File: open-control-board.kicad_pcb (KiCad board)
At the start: 4 copper layers, 69 x 109 mm, 140 parts, among them CN1 Service boiler fill sensor, CN10 LCC Port, CN2 Water tank level switch, CN3 NTC Service Boiler, CN4 NTC Brew Boiler, CN5 Service boiler relay, CN6 Conn_02x04_Counter_Clockwise, CN7 Brew Switch, CN8 12V Separate Supply, CN9 Brew boiler relay, J1 USB_B_Micro, J10 Conn_01x04_Pin, J11 Conn_01x04_Pin, J12 Conn_02x06_Odd_Even, J13 Conn_02x05_Odd_Even, J14 Conn_02x04_Odd_Even, J15 Conn_02x05_Odd_Even, J16 USB_B_Micro, J17 BM04B-SRSS-TB(LF)(SN), J2 BM04B-SRSS-TB(LF)(SN), J3 Conn_01x01_Pin, J4 Conn_01x01_Pin, J5 Conn_01x01_Pin, J6 Conn_01x01_Pin, J7 Conn_01x01_Pin, J8 Conn_01x01_Pin, J9 ECE05US05, K1 RT314A12, Q1 AO3401A, Q2 AO3401A, Q3 AO3401A, Q4 AO3401A, Q5 AO3401A, SW1 SW_Push, SW2 SW_Push, SW3 SW_Push, SW4 SW_Push, U1 TPS82130, U10 FDC1004, U11 ALDP112, U12 ALDP112, U13 ALDP112, U15 STPIC6C595TTR, U16 STPIC6C595TTR, U2 MCP7940N-xSN, U3 TPS82130, U4 RP2040, U5 ESP32-S3-WROOM-1, U7 TXB0108DQSR, U8 ADS1115IDGS, U9 W25Q16JVUXIQ, Y1 XYDBPCNANF-12MHZ, Y3 YSX1610SK, 9 pF

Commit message: WIP
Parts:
- added locked: VAL**, Panelization:mouse-bite-2mm-slot, F.Cu at (55.8, 79.5)
- added mouse-bite-2mm-slot: VAL**, Panelization:mouse-bite-2mm-slot, F.Cu at (96.8, 79.5)
- added mouse-bite-2mm-slot: VAL**, Panelization:mouse-bite-2mm-slot, F.Cu at (75.2, 79.5)
- added mouse-bite-2mm-slot: VAL**, Panelization:mouse-bite-2mm-slot, F.Cu at (117.3, 79.5)
- C32: value 22 uF, 10V, X5R -> 22 uF, 6.3V, X5R
- FB1, FB2: footprint PCM_Ferrite_SMD_AKL:Ferrite_0402_1005Metric -> PCM_Ferrite_SMD_AKL:Ferrite_0603_1608Metric
- J3, J4, J5, J6, J7, J8: footprint Connector_Pin:Pin_D1.4mm_L8.5mm_W2.8mm_FlatFork -> 1289:KEYSTONE_1289
- moved J8 5.02 mm to (110.0, 128.6), turned to 90 degrees
- moved J5 4.45 mm to (68.6, 128.6), turned to 90 degrees
- moved F1 1.00 mm to (110.0, 121.0)
- moved J9 1.00 mm to (98.1, 113.8)
- moved JP1 1.00 mm to (54.3, 83.0)
- moved K1 1.00 mm to (56.2, 91.8)
- moved U11 1.00 mm to (90.8, 115.8)
- moved U12 1.00 mm to (82.3, 115.8)
- moved U13 1.00 mm to (73.8, 115.8)
- moved C29 0.93 mm to (97.3, 32.8)
- moved R27 0.92 mm to (100.8, 33.6)
- moved J6 0.89 mm to (56.2, 128.4), turned to 90 degrees
- moved J4 0.80 mm to (82.7, 129.2), turned to 90 degrees
- moved J7 0.77 mm to (103.2, 128.8), turned to 90 degrees
- moved FB2 0.68 mm to (98.5, 35.0)
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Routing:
- net +3V3: track 271.6 -> 321.3 mm, vias 11 -> 12
- net GND: track 99.9 -> 119.4 mm, vias 50 -> 34
- net nG_5V: track 8.97 -> 19.8 mm
- net ESP32_RP2040_UART2: track 17.8 -> 26.2 mm
- net SRCLR_5V: track 10.7 -> 18.9 mm
- net CN6_3_5V: track 25.7 -> 33.6 mm
- net CN6_2_5V: track 21.3 -> 28.7 mm
- net WATER_TANK_LVL_SW: track 16.4 -> 23.0 mm, vias 1 -> 2
- net RCLK_5V: track 11.5 -> 18.0 mm
- net GP27: track 36.3 -> 42.5 mm
- net GP26: track 40.9 -> 47.0 mm
- net SRCK_3V3: track 25.1 -> 31.0 mm
- net SRCK_5V: track 14.1 -> 19.6 mm, vias 2 -> 0
- net SRCLR_3V3: track 22.0 -> 27.4 mm
- net SER_IN_3V3: track 22.9 -> 28.0 mm
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- added copper zone on In2.Cu, net GND
- removed copper zone on In2.Cu, net (none)
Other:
- board size 69 x 109 mm -> 69 x 110 mm

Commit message: WIP
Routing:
- net Net-(U16-DRAIN1): track 50.5 -> 47.8 mm
- net SRCK_5V: track 19.6 -> 17.2 mm
- net SRCK_3V3: track 31.0 -> 33.3 mm
- net nG_5V: track 19.8 -> 17.7 mm
- net GP21: track 49.2 -> 47.7 mm
- net SRCLR_5V: track 18.9 -> 20.2 mm
- net Net-(U15-DRAIN1): track 45.9 -> 44.7 mm
- net CN10_12V_GATE: track 50.9 -> 49.8 mm
- net Net-(U16-DRAIN0): track 36.5 -> 35.5 mm
- net ESP32_RP2040_UART1: track 34.7 -> 33.6 mm, vias 4 -> 2
- net CN10_UART_RX: track 69.9 -> 68.9 mm
- net RP2040_BOOTSEL: track 29.0 -> 29.8 mm
- net ESP32_EN: track 47.6 -> 46.9 mm
- net Net-(U15-DRAIN5): track 6.32 -> 5.56 mm
- net RCLK_3V3: track 23.0 -> 22.4 mm
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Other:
- board text added: "12V"
- board text added: "3V3"
- board text added: "5V"
- board text added: "AGND"
- board text added: "AVCC"
- board text added: "ESP32 EN"
- board text added: "ESP32 GPIO0"
- board text added: "ESP32 JTAG"
- board text added: "ESP32 JTAG Source"
- board text added: "ESP32 QWIIC"
- board text added: "ESP32 USB"
- board text added: "GND"
- board text added: "RP2040 Boot"
- board text added: "RP2040 DBG"
- board text added: "RP2040 QWIIC"
- board text added: "RP2040 Reset"
- board text added: "RP2040 USB"
- board text added: "USB 5V"
- board text added: "VOUT1 V"
- board text added: "VOUT2 V"
- board text added: "VOUT3 V"

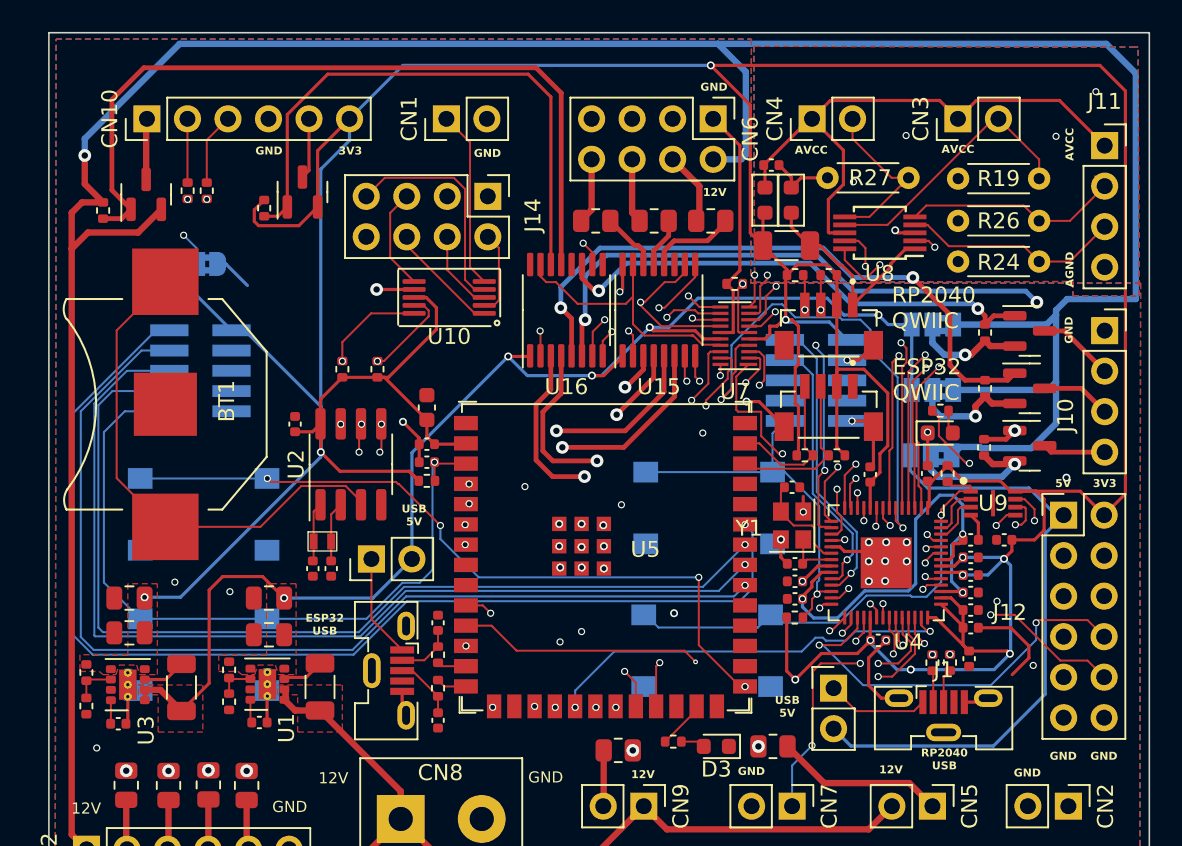
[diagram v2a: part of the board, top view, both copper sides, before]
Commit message: Added possibility to select CN10 levels via solder jumpers
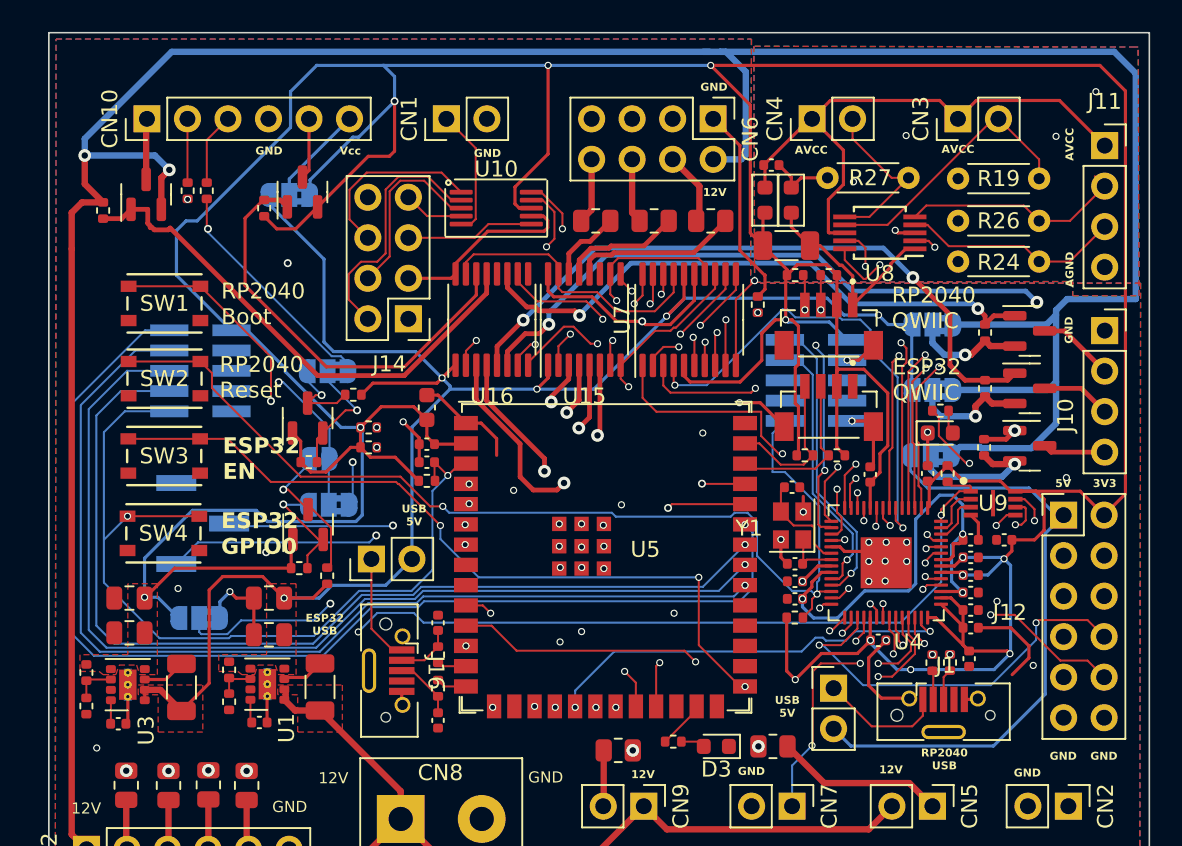
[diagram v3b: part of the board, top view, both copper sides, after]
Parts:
- removed BT1: Battery_Cell, BK-885:BAT_BK-885
- removed C24, C25: 11 pF, Capacitor_SMD:C_0402_1005Metric
- removed C26: 100 nF, 50V, X7R, Capacitor_SMD:C_0402_1005Metric
- removed U2: MCP7940N-xSN, Package_SO:SOP-8_3.76x4.96mm_P1.27mm
- removed Y3: YSX1610SK, 9 pF, SMD1610-2P:SMD1610-2P
- added J18: Conn_01x03_Pin, Connector_PinHeader_2.54mm:PinHeader_1x03_P2.54mm_Vertical_SMD_Pin1Left, B.Cu at (61.6, 55.3)
- added JP10: SolderJumper_3_Bridged12, Jumper:SolderJumper-3_P1.3mm_Bridged2Bar12_RoundedPad1.0x1.5mm_NumberLabels, B.Cu at (69.5, 45.7)
- added JP11: SolderJumper_3_Bridged12, Jumper:SolderJumper-3_P1.3mm_Bridged2Bar12_RoundedPad1.0x1.5mm_NumberLabels, B.Cu at (69.5, 54.1)
- added JP12: SolderJumper_2_Open, Jumper:SolderJumper-2_P1.3mm_Open_RoundedPad1.0x1.5mm, B.Cu at (68.9, 51.2)
- added JP9: SolderJumper_3_Bridged12, Jumper:SolderJumper-3_P1.3mm_Bridged2Bar12_RoundedPad1.0x1.5mm_NumberLabels, B.Cu at (67.1, 34.7)
- added Q6: 2N7002, Package_TO_SOT_SMD:SOT-23, F.Cu at (68.2, 48.7)
- added Q7: 2N7002, Package_TO_SOT_SMD:SOT-23, F.Cu at (68.2, 55.3)
- added R41: 10K, Resistor_SMD:R_0402_1005Metric, F.Cu at (68.3, 51.4)
- added R42: 10K, Resistor_SMD:R_0402_1005Metric, F.Cu at (71.1, 47.2)
- added R43: 10K, Resistor_SMD:R_0402_1005Metric, F.Cu at (67.7, 58.1)
- added R44: 10K, Resistor_SMD:R_0402_1005Metric, F.Cu at (69.5, 58.5)
- J1, J16: footprint Connector_USB:USB_Micro-B_Molex-105133-0031 -> U-D-M5DS-W-3:U-D-M5DS-W-3
- JP4, JP5, JP6: footprint Jumper:SolderJumper-3_P1.3mm_Bridged2Bar12_Pad1.0x1.5mm_NumberLabels -> Jumper:SolderJumper-3_P1.3mm_Bridged2Bar12_RoundedPad1.0x1.5mm_NumberLabels
- SW1, SW2, SW3, SW4: footprint Button_Switch_SMD:SW_SPST_B3S-1000 -> ul_PTS815-SJM-250-SMTR-LFS:SW4_PTS815 SJM 250 SMTR LFS_CNK; moved to F.Cu
- U7: value TXB0108DQSR -> TXB0108PWR; footprint Package_SON:USON-20_2x4mm_P0.4mm -> Package_SO:TSSOP-20_4.4x6.5mm_P0.65mm
- moved SW1 40.4 mm to (59.2, 41.5), turned to 0 degrees
- moved SW2 35.1 mm to (59.3, 46.2), turned to 0 degrees
- moved JP8 22.2 mm to (61.4, 61.2)
- moved J14 9.15 mm to (74.5, 42.4), turned to 180 degrees
- moved SW4 8.01 mm to (59.2, 55.9), turned to 0 degrees
- moved U10 6.33 mm to (80.0, 35.5), turned to 0 degrees
- moved R21 4.93 mm to (72.0, 50.5), turned to 180 degrees
- moved U15 4.71 mm to (85.6, 42.5)
- moved U16 4.71 mm to (79.8, 42.5)
- moved SW3 4.41 mm to (59.2, 51.0), turned to 0 degrees
- moved R20 4.01 mm to (72.0, 49.2), turned to 180 degrees
- moved U7 3.03 mm to (92.2, 42.5), turned to 90 degrees
- moved R31 1.95 mm to (96.5, 41.5), turned to 90 degrees
- moved J16 1.25 mm to (72.1, 64.5)
- moved J1 1.05 mm to (108.1, 68.3)
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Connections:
- CN10 pad 6: +3V3 -> Net-(CN10-Pin_6)
- R5 pad 2: CN10_UART_TX -> CN10_UART_RX
- R6 pad 2: CN10_UART_RX -> CN10_UART_TX_SHIFT_SEL
- U4 pad 18: RTC_MFP -> GP15
- U4 pad 28: CN10_UART_RX -> CN10_UART_RX_SHIFT_SEL
- U5 pad 10: CN10_UART_RX -> CN10_UART_RX_SHIFT_SEL
- U5 pad 36: ESP32_RXD0 -> Net-(J18-Pin_1)
- U5 pad 37: ESP32_TXD0 -> Net-(J18-Pin_2)
- U5 pad 8: ESP32_RTS0 -> unconnected-(U5-GPIO15/U0RTS/ADC2_CH4/XTAL_32K_P-Pad8)
- U5 pad 9: ESP32_CTS0 -> unconnected-(U5-GPIO16/U0CTS/ADC2_CH5/XTAL_32K_N-Pad9)
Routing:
- net CN10_UART_RX_SHIFT_SEL: track 0.00 -> 56.3 mm, vias 0 -> 4
- net RP2040_BOOTSEL: track 29.8 -> 77.8 mm, vias 1 -> 3
- net CN10_UART_RX: track 68.9 -> 23.0 mm, vias 4 -> 2
- net RP2040_RESETn: track 23.7 -> 67.0 mm, vias 1 -> 2
- net Net-(J18-Pin_1): track 0.00 -> 39.8 mm, vias 0 -> 2
- net +3V3: track 321.2 -> 358.1 mm, vias 12 -> 14
- net RTC_MFP: track 36.3 -> 0.00 mm, vias 2 -> 0
- net Net-(J18-Pin_2): track 0.00 -> 35.0 mm, vias 0 -> 2
- net GND: track 119.1 -> 153.7 mm, vias 34 -> 35
- net Net-(BT1-+): track 32.1 -> 0.00 mm
- net +5V: track 125.5 -> 151.3 mm
- net CN10_12V_GATE: track 49.8 -> 32.6 mm
- net CN10_UART_TX_SHIFT_SEL: track 0.00 -> 14.8 mm, vias 0 -> 1
- net ESP32_JTAG_SELECT: track 39.8 -> 28.2 mm
- net CIN1: track 5.32 -> 15.8 mm
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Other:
- board text added: "Bridged = 5V"
- board text added: "CN10 RX V"
- board text added: "CN10 TX V"
- board text added: "CN10 Vcc"
- board text added: "RX"
- board text added: "TX"
- board text added: "UART"
- board text added: "Vcc"

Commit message: WIP
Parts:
- removed JP10, JP11: SolderJumper_3_Bridged12, Jumper:SolderJumper-3_P1.3mm_Bridged2Bar12_RoundedPad1.0x1.5mm_NumberLabels
- removed JP12: SolderJumper_2_Open, Jumper:SolderJumper-2_P1.3mm_Open_RoundedPad1.0x1.5mm
- removed Q7: 2N7002, Package_TO_SOT_SMD:SOT-23
- removed R41, R42, R43, R44: 10K, Resistor_SMD:R_0402_1005Metric
- added JP13: SolderJumper_3_Bridged12, Jumper:SolderJumper-3_P1.3mm_Bridged2Bar12_RoundedPad1.0x1.5mm_NumberLabels, B.Cu at (98.3, 37.0)
- added Q11: DMN63D8LDW, PCM_Package_TO_SOT_SMD_AKL:SOT-363_SC-70-6, F.Cu at (61.8, 34.7)
- added R49: 10K, Resistor_SMD:R_0402_1005Metric, F.Cu at (115.3, 42.1)
- added R50: 10K, Resistor_SMD:R_0402_1005Metric, F.Cu at (113.3, 39.9)
- added REF**: OSHW-Logo2_14.6x12mm_SilkScreen, Symbol:OSHW-Logo2_14.6x12mm_SilkScreen, F.Cu at (83.5, 89.0)
- added REF**: OSHW-Logo2_7.3x6mm_Copper, Symbol:OSHW-Logo2_7.3x6mm_Copper, B.Cu at (57.2, 37.9)
- added RN1: 10K, PCM_Resistor_SMD_AKL:R_Array_Concave_4x0402, F.Cu at (61.9, 37.3)
- added RN2: 10K, PCM_Resistor_SMD_AKL:R_Array_Concave_4x0402, F.Cu at (113.3, 41.7)
- Q3, Q5: value AO3401A -> Q_PMOS-E_DUAL_Generic_SEP_S1G1D2S2G2D1; footprint Package_TO_SOT_SMD:SOT-23 -> PCM_Package_TO_SOT_SMD_AKL:Vishay_PowerPAK_SC70-6L_Dual
- Q4: value AO3401A -> DMN63D8LDW; footprint Package_TO_SOT_SMD:SOT-23 -> PCM_Package_TO_SOT_SMD_AKL:SOT-363_SC-70-6
- Q6: value 2N7002 -> DMN63D8LDW; footprint Package_TO_SOT_SMD:SOT-23 -> PCM_Package_TO_SOT_SMD_AKL:SOT-363_SC-70-6
- moved Q6 39.8 mm to (107.5, 42.0)
- moved R29 6.75 mm to (114.5, 52.4), turned to 0 degrees
- moved R30 4.76 mm to (114.9, 48.4), turned to 180 degrees
- moved R28 4.35 mm to (115.0, 44.2), turned to 180 degrees
- moved Q5 4.21 mm to (114.6, 46.3), turned to 90 degrees
- moved Q3 3.83 mm to (114.6, 50.5), turned to 90 degrees
- moved Q4 3.32 mm to (110.4, 42.0), turned to 90 degrees
- moved JP6 2.79 mm to (110.1, 51.2)
- moved JP4 2.74 mm to (110.0, 43.6)
- moved JP5 2.69 mm to (110.0, 47.4)
- moved R6 2.04 mm to (62.9, 32.6), turned to 180 degrees
- moved R5 1.77 mm to (60.9, 32.6), turned to 0 degrees
- moved R24 0.68 mm to (109.0, 38.2)
- moved R19 0.38 mm to (109.0, 35.9)
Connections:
- net Net-(CN10-Pin_6) renamed CN10_UART_VCC
- C28 pad 1: +3V3 -> Net-(JP13-C)
- FB1 pad 2: +3V3 -> Net-(JP13-C)
- J12 pad 1: +5V -> +3V3
- Q3 pad 1: VOUT_2_GATE -> Net-(JP5-C)
- Q3 pad 2: Net-(JP5-C) -> VOUT_2_GATE
- Q3 pad 3: VOUT_2 -> VOUT_3
- Q4 pad 1: VOUT_1_GATE -> ADS1115_RDY
- Q4 pad 2: Net-(JP4-C) -> +3V3
- Q4 pad 3: VOUT_1 -> unconnected-(Q4B-D2-Pad3)
- Q5 pad 1: VOUT_3_GATE -> (no net)
- Q5 pad 2: Net-(JP6-C) -> (no net)
- Q5 pad 3: VOUT_3 -> VOUT_1
- Q6 pad 1: +3V3 -> INT_SDA
- Q6 pad 2: CN10_UART_TX -> +3V3
- Q6 pad 3: Net-(JP10-B) -> INT_SCL_AVCC
- U8 pad 1: GND -> AGND
- U8 pad 10: INT_SCL -> INT_SCL_AVCC
- U8 pad 2: ADS1115_RDY -> ADS1115_RDY_AVCC
- U8 pad 9: INT_SDA -> INT_SDA_AVCC
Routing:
- net AGND: track 5.56 -> 25.2 mm
- net CN10_UART_RX_SHIFT_SEL: track 56.3 -> 75.6 mm
- net VOUT_2_GATE: track 41.7 -> 60.6 mm
- net CN10_UART_RX: track 23.0 -> 5.28 mm, vias 2 -> 0
- net +12V: track 249.6 -> 233.2 mm
- net INT_SCL_AVCC: track 0.00 -> 14.4 mm, vias 0 -> 2
- net AVCC: track 37.0 -> 51.3 mm
- net INT_SDA_AVCC: track 0.00 -> 14.3 mm, vias 0 -> 2
- net CN10_UART_TX: track 61.7 -> 73.2 mm, vias 4 -> 5
- net CN10_UART_VCC: track 6.66 -> 17.2 mm, vias 0 -> 1
- net ADS1115_RDY_AVCC: track 0.00 -> 9.31 mm
- net Net-(JP12-B): track 9.17 -> 0.00 mm, vias 1 -> 0
- net VOUT_3_GATE: track 49.2 -> 56.5 mm, vias 3 -> 2
- net Net-(JP11-B): track 7.18 -> 0.00 mm, vias 1 -> 0
- net VOUT_1_GATE: track 36.9 -> 43.6 mm
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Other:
- board text added: "ADC Vcc"
- board text added: "All-Purpose Espresso Controller HV board"
- board text added: "All-Purpose Espresso Controller Main board"
- board text added: "Are there reasonable fuses for this footprint?"
- board text added: "ESP32"
- board text added: "Height???"
- board text added: "RP2040"
- board text added: "Rename connectors and jumpers?"
- board text added: "Rev R0A"
- board text added: "Split ground?"
- board text added: "The drill size looks small, but is according to the Data sheet. Double check though."
- board text added: "This part still needs to be measured to a case"
- board text removed: "Bridged = 5V"
- board text removed: "CN10 RX V"
- board text removed: "CN10 TX V"
- board text removed: "ESP32 QWIIC"
- board text removed: "RP2040 QWIIC"

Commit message: WIP
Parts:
- removed J9: ECE05US05, ECE05:CONN5_05US05_XPP
- removed R14, R15, R16, R25, R3, R38, R39, R4, R40: 480R, 500mW, Resistor_SMD:R_0805_2012Metric
- removed REF**: OSHW-Logo2_14.6x12mm_SilkScreen, Symbol:OSHW-Logo2_14.6x12mm_SilkScreen
- removed REF**: OSHW-Logo2_7.3x6mm_Copper, Symbol:OSHW-Logo2_7.3x6mm_Copper
- added C24: 100 nF, 50V, X7R, Capacitor_SMD:C_0402_1005Metric, F.Cu at (82.3, 32.7)
- added C25: 1 uF, 16V, X5R, Capacitor_SMD:C_0402_1005Metric, F.Cu at (82.4, 33.8)
- added D2: 1N4001, Diode_THT:D_DO-41_SOD81_P7.62mm_Horizontal, F.Cu at (91.3, 93.3)
- added D4: 1N4001, Diode_THT:D_DO-41_SOD81_P7.62mm_Horizontal, F.Cu at (83.3, 89.2)
- added D5: 1N4001, Diode_THT:D_DO-41_SOD81_P7.62mm_Horizontal, F.Cu at (75.9, 93.3)
- added D8: 1N4001, Diode_THT:D_DO-41_SOD81_P7.62mm_Horizontal, F.Cu at (54.6, 87.2)
- added U2: ~, ECE05:ECE10, F.Cu at (119.6, 82.6)
- F1: value Fuse -> Schurter FRT 250T 7100.1009.13; footprint Fuse:Fuse_Bourns_MF-RG700 -> 1289:FRT 250T
- J3, J4, J5, J6, J7, J8: value Conn_01x01_Pin -> TE 160650-2
- Q3, Q5: footprint PCM_Package_TO_SOT_SMD_AKL:Vishay_PowerPAK_SC70-6L_Dual -> PCM_Package_TO_SOT_SMD_AKL:TSOT-23-6
- U9: footprint W25Q16JVUXIQ:SON50P300X200X60-9N -> ul_W25Q16JVUXIQ:W25Q16JVUXIQ_WIN
- moved F1 12.9 mm to (107.1, 133.6), turned to 90 degrees
- moved J3 10.7 mm to (80.0, 129.0)
- moved J4 10.2 mm to (72.5, 129.0)
- moved J7 8.25 mm to (95.0, 129.0)
- moved J6 6.28 mm to (62.5, 129.0)
- moved J8 5.01 mm to (115.0, 129.0)
- moved R30 4.78 mm to (111.2, 51.4), turned to -90 degrees
- moved R28 4.58 mm to (111.0, 46.6), turned to -90 degrees
- moved R29 4.55 mm to (111.2, 49.3), turned to -90 degrees
- moved J5 1.17 mm to (67.5, 129.0)
- moved R35 0.90 mm to (90.3, 68.8)
- moved D3 0.90 mm to (93.0, 69.1)
- moved Q3 0.79 mm to (113.9, 50.9), turned to 0 degrees
- moved U10 0.77 mm to (80.0, 36.3)
- moved Q5 0.66 mm to (114.0, 46.1), turned to 0 degrees
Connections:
- CN1 pad 1: CIN4 -> CIN1
- F1 pad 1: Net-(J8-Pin_1) -> PH_PRE_FUSE
- J14 pad 2: CIN1 -> C_SHIELD_2
- J14 pad 3: GND -> C_SHIELD_2
- J14 pad 4: CIN2 -> CIN4
- J14 pad 5: C_SHIELD_2 -> CIN3
- J14 pad 7: CIN3 -> CIN2
- J14 pad 8: GND -> C_SHIELD_1
- J7 pad 1: N -> PH_PRE_FUSE
- J8 pad 1: Net-(J8-Pin_1) -> N
- Q3 pad 1: Net-(JP5-C) -> VOUT_2_GATE
- Q3 pad 2: VOUT_2_GATE -> Net-(JP6-C)
- Q3 pad 3: VOUT_3 -> VOUT_3_GATE
- Q3 pad 4: Net-(JP6-C) -> VOUT_3
- Q3 pad 5: VOUT_3_GATE -> Net-(JP5-C)
- Q5 pad 2: (no net) -> Net-(JP4-C)
- Q5 pad 3: VOUT_1 -> VOUT_1_GATE
- Q5 pad 4: Net-(JP4-C) -> VOUT_1
- Q5 pad 5: VOUT_1_GATE -> (no net)
- U15 pad 12: Net-(U15-DRAIN5) -> CN6_4
- U15 pad 13: Net-(U15-DRAIN6) -> CN6_6
- U15 pad 14: Net-(U15-DRAIN7) -> CN6_8
- U15 pad 3: Net-(U15-DRAIN0) -> JP2_FA10
- U15 pad 4: Net-(U15-DRAIN1) -> JP2_FA9
- U15 pad 5: Net-(U15-DRAIN2) -> JP2_FA8
- U15 pad 6: Net-(U15-DRAIN3) -> JP2_FA7
- U16 pad 3: Net-(U16-DRAIN0) -> CN9_DRAIN
- U16 pad 4: Net-(U16-DRAIN1) -> CN5_DRAIN
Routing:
- net CN5_DRAIN: track 10.6 -> 55.4 mm, vias 0 -> 2
- net Net-(U16-DRAIN1): track 43.0 -> 0.00 mm, vias 2 -> 0
- net JP2_FA10: track 3.12 -> 45.8 mm, vias 0 -> 1
- net JP2_FA9: track 3.11 -> 45.2 mm, vias 0 -> 1
- net JP2_FA8: track 3.13 -> 45.0 mm, vias 0 -> 1
- net JP2_FA7: track 3.14 -> 44.6 mm, vias 0 -> 1
- net Net-(U15-DRAIN0): track 40.7 -> 0.00 mm, vias 2 -> 0
- net Net-(U15-DRAIN1): track 40.3 -> 0.00 mm, vias 2 -> 0
- net Net-(U15-DRAIN2): track 40.0 -> 0.00 mm, vias 2 -> 0
- net Net-(U15-DRAIN3): track 39.8 -> 0.00 mm, vias 2 -> 0
- net CN9_DRAIN: track 3.51 -> 39.1 mm, vias 0 -> 2
- net Net-(U16-DRAIN0): track 35.6 -> 0.00 mm, vias 2 -> 0
- net +12VA: track 58.3 -> 90.2 mm
- net C_SHIELD_2: track 8.07 -> 27.2 mm
- net PH_PRE_FUSE: track 0.00 -> 14.8 mm
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- added copper zone on B.Cu, net C_SHIELD_1
- added copper zone on In1.Cu, net C_SHIELD_1
- added copper zone on In2.Cu, net C_SHIELD_1
- added copper zone on B.Cu, net C_SHIELD_2
- added copper zone on In1.Cu, net C_SHIELD_2
- added copper zone on In2.Cu, net C_SHIELD_2
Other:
- board text added: "Connector height: 10.16 mm over board"
- board text added: "Height: <16 mm over board"
- board text removed: "Are there reasonable fuses for this footprint?"
- board text removed: "Height???"
- board text removed: "The drill size looks small, but is according to the Data sheet. Double check though."
- board text removed: "This part still needs to be measured to a case"
